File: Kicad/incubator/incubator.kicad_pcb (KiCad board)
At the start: 2 copper layers, 99.1 x 73.7 mm, 44 parts, among them J1 Barrel_Jack_MountingPin, J2 Conn_01x06, J3 Conn_01x01, J4 RJ12, J5 Conn_01x01, J6 Conn_01x01, J7 Conn_01x01, SW2 Rotary_Encoder_Switch, U1 ACT4088, U2 ATmega328P-AU

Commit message: refactor: final test version
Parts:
- removed C3, C4: 22µF, Capacitor_SMD:C_0805_2012Metric_Pad1.18x1.45mm_HandSolder
- removed H5, H6, H7, H8: MountingHole, MountingHole:MountingHole_4.5mm
- removed L1: 4.7µH, Inductor_SMD:L_Taiyo-Yuden_NR-40xx_HandSoldering
- removed R10: 1k, Resistor_SMD:R_0805_2012Metric_Pad1.20x1.40mm_HandSolder
- removed R9: 10k, Resistor_SMD:R_0805_2012Metric_Pad1.20x1.40mm_HandSolder
- added J8: Conn_02x03_Odd_Even, Connector:Tag-Connect_TC2030-IDC-NL_2x03_P1.27mm_Vertical, F.Cu at (65.7, -42.9)
- added logoHackuarium: , incubator:logoHackuarium, F.Cu at (87.1, -61.1)
- C1: value 10µF -> 0.33U
- C2: value 22nF -> 0.1U
- D1: value MBR0520LT -> GREEN; footprint Diode_SMD:D_SOD-123 -> LED_SMD:LED_0805_2012Metric_Pad1.15x1.40mm_HandSolder
- D3: value GREEN -> MBR0520LT; footprint LED_SMD:LED_0805_2012Metric_Pad1.15x1.40mm_HandSolder -> Diode_SMD:D_SOD-123
- J3, J5, J6, J7: moved to B.Cu
- R3: value 9.64k -> 10k
- R4: value 49.9k -> 1k
- RV1: moved to F.Cu
- U1: value ACT4088 -> LM78M05_TO252; footprint Package_TO_SOT_SMD:SOT-23-6_Handsoldering -> Package_TO_SOT_SMD:TO-252-2
- moved J4 81.2 mm to (89.8, -32.5), turned to 270 degrees
- moved R2 69.2 mm to (83.7, -32.6), turned to 0 degrees
- moved R1 68.5 mm to (83.7, -30.2), turned to 0 degrees
- moved D3 43.5 mm to (64.4, -47.8), turned to 270 degrees
- moved J7 40.0 mm to (39.4, -23.7), turned to 0 degrees
- moved J6 32.1 mm to (45.9, -23.7), turned to 0 degrees
- moved J3 26.4 mm to (52.5, -23.7), turned to 0 degrees
- moved J5 18.6 mm to (59.0, -23.7), turned to 0 degrees
- moved C1 14.1 mm to (16.9, -52.7)
- moved R4 11.5 mm to (26.9, -56.5), turned to 90 degrees
- moved R7 11.4 mm to (5.45, -33.4)
- moved R8 11.4 mm to (5.45, -44.8)
- moved D1 10.9 mm to (14.0, -61.0), turned to 270 degrees
- moved C2 9.48 mm to (23.7, -52.7)
- moved D4 9.27 mm to (24.4, -49.9), turned to 180 degrees
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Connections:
- C2 pad 2: Net-(C2-Pad2) -> GND
- D1 pad 1: Net-(C2-Pad2) -> GND
- D1 pad 2: GND -> Net-(D1-Pad2)
- D3 pad 1: GND -> VIN
- D4 pad 2: /5 V Step-down/5V -> Net-(C2-Pad1)
- R3 pad 1: GND -> 12V
- R3 pad 2: Net-(R3-Pad2) -> Net-(D1-Pad2)
- R4 pad 1: /5 V Step-down/5V -> VIN
- R4 pad 2: Net-(R3-Pad2) -> Net-(D2-Pad2)
- U1 pad 1: Net-(C2-Pad2) -> 12V
- U1 pad 2: 12V -> GND
- U1 pad 3: Net-(U1-Pad3) -> Net-(C2-Pad1)
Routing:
- net SDA: track 128.2 -> 77.6 mm, vias 2 -> 3
- net SCL: track 130.8 -> 81.0 mm, vias 2 -> 4
- net ~RESET: track 36.6 -> 75.3 mm, vias 1 -> 2
- net /5 V Step-down/5V: track 22.8 -> 0.00 mm
- net 12V: track 201.5 -> 222.9 mm
- net D5: track 76.8 -> 57.4 mm
- net D6: track 78.4 -> 59.2 mm
- net D7: track 64.2 -> 45.2 mm
- net SCK: track 0.00 -> 18.5 mm, vias 0 -> 2
- net MOSI: track 0.00 -> 15.3 mm, vias 0 -> 2
- net MISO: track 0.00 -> 13.5 mm
- net C3: track 135.1 -> 147.7 mm
- net Net-(C2-Pad2): track 9.84 -> 0.00 mm
- net Net-(R3-Pad2): track 4.97 -> 0.00 mm
- net VIN: track 130.7 -> 134.7 mm, vias 2 -> 4
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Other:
- board size 99.1 x 73.7 mm -> 99.9 x 73.7 mm
- board text added: "5V"
- board text added: "GND"
- board text added: "Incubator V 1.0.0"
- board text added: "SCL"
- board text added: "SDA"
- board text added: "VCC"
- board text added: "⏚"

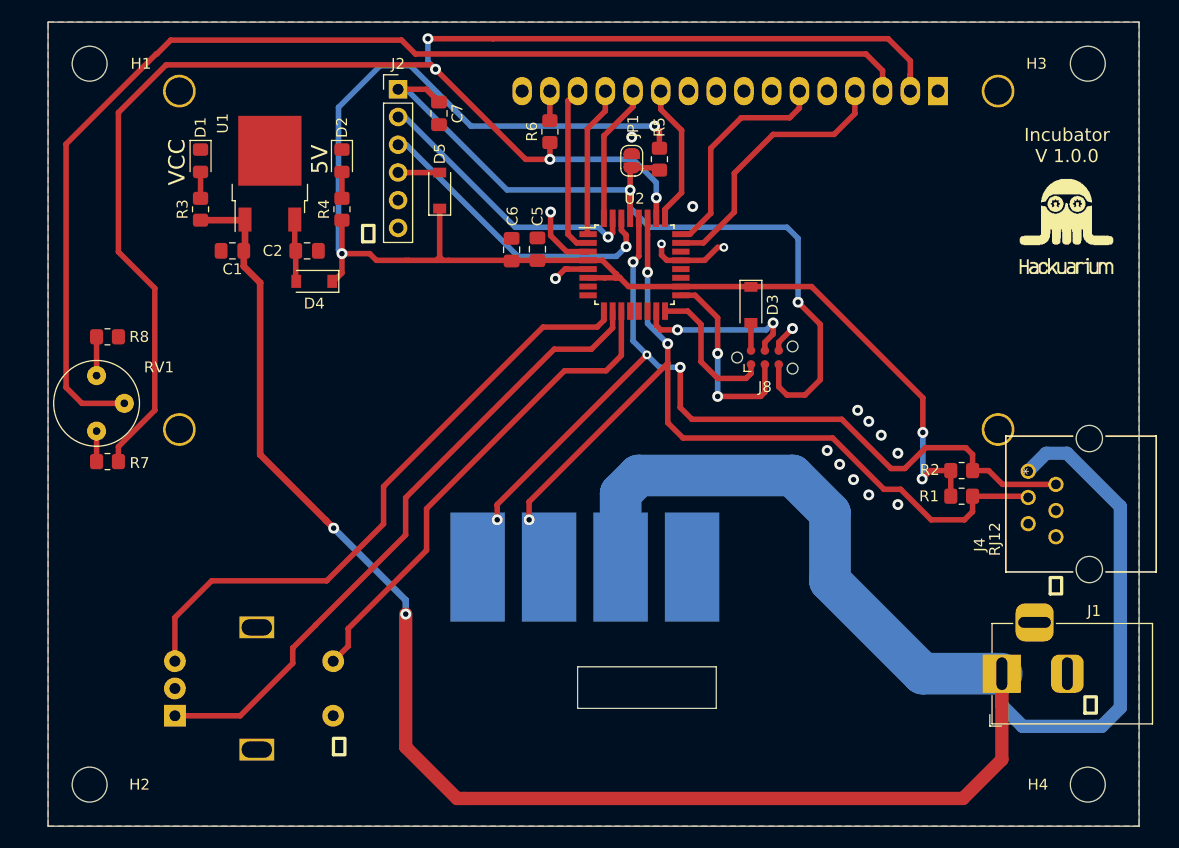
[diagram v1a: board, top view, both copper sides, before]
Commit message: fix: iss #1: add ERROR and BLINKING LED, iss #2: solved
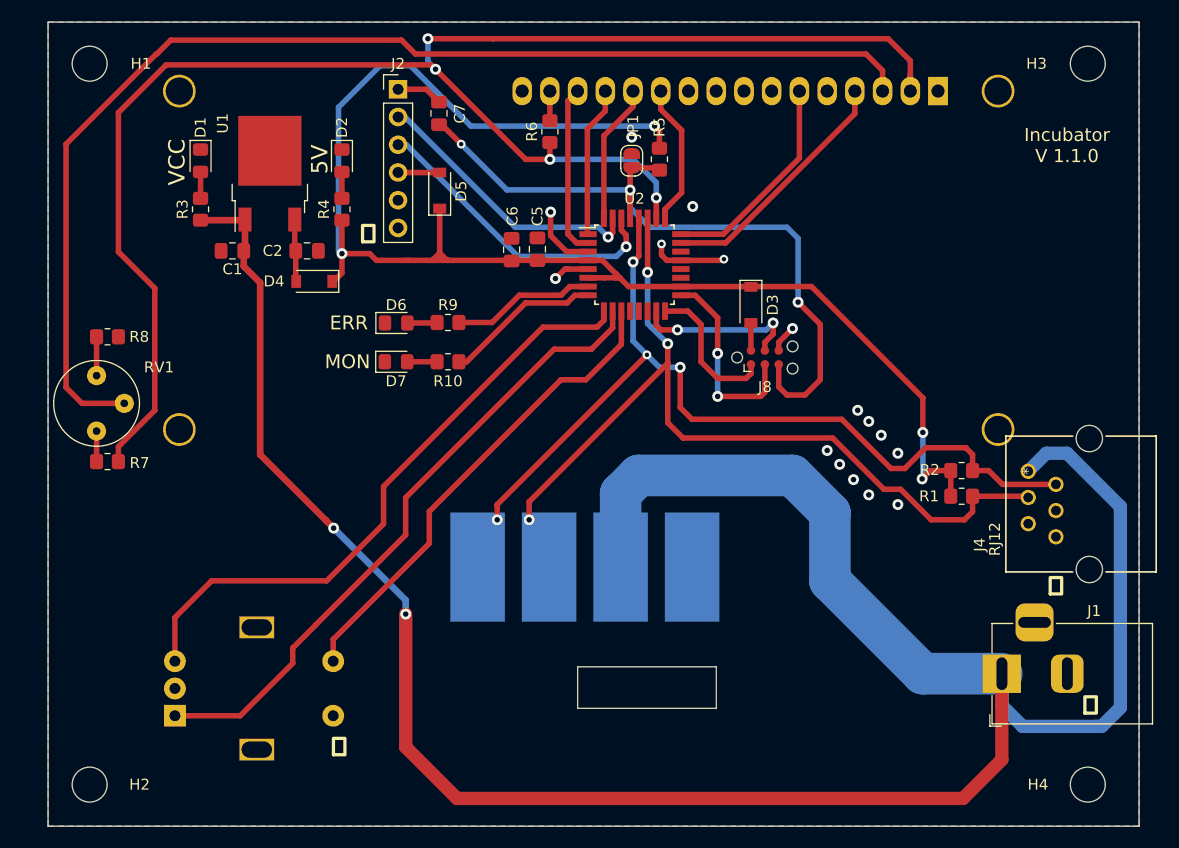
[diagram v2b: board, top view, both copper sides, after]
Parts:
- removed logoHackuarium: , incubator:logoHackuarium
- added D6: GREEN, LED_SMD:LED_0805_2012Metric_Pad1.15x1.40mm_HandSolder, F.Cu at (31.9, -46.1)
- added D7: GREEN, LED_SMD:LED_0805_2012Metric_Pad1.15x1.40mm_HandSolder, F.Cu at (31.9, -42.5)
- added R10: 1k, Resistor_SMD:R_0805_2012Metric_Pad1.20x1.40mm_HandSolder, F.Cu at (36.6, -42.5)
- added R9: 1k, Resistor_SMD:R_0805_2012Metric_Pad1.20x1.40mm_HandSolder, F.Cu at (36.6, -46.1)
- C1: value 0.33U -> 0.33u
- C2: value 0.1U -> 100n
- D1, D2: value GREEN -> RED
- turned C7 to 90 degrees
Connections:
- C7 pad 2: GND -> Net-(C7-Pad2)
- J2 pad 1: ~RESET -> Net-(C7-Pad2)
- U2 pad 7: Net-(U2-Pad7) -> ERROR
- U2 pad 8: Net-(U2-Pad8) -> MONITORING
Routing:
- net MONITORING: track 0.00 -> 14.4 mm
- net ERROR: track 0.00 -> 13.2 mm
- net ~RESET: track 75.3 -> 66.0 mm, vias 2 -> 3
- net Net-(C7-Pad2): track 0.00 -> 4.23 mm
- net Net-(D6-Pad2): track 0.00 -> 2.74 mm
- net Net-(D7-Pad2): track 0.00 -> 2.74 mm
- net C0: track 25.0 -> 22.9 mm
- net VIN: track 134.7 -> 136.8 mm
- net D7: track 45.2 -> 44.3 mm
- net C1: track 20.7 -> 19.9 mm
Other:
- board text added: "ERR"
- board text added: "Incubator V 1.1.0"
- board text added: "MON"
- board text removed: "Incubator V 1.0.0"
